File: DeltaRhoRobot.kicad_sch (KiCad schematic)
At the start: 44 parts, among them J11 Conn_01x02_Socket, J5 USB_C_Receptacle_USB2.0, J6 USB_C_Receptacle_USB2.0, SW1 CAS-120A1, U2 AMS1117-3.3, U7 TPS566242DRLR

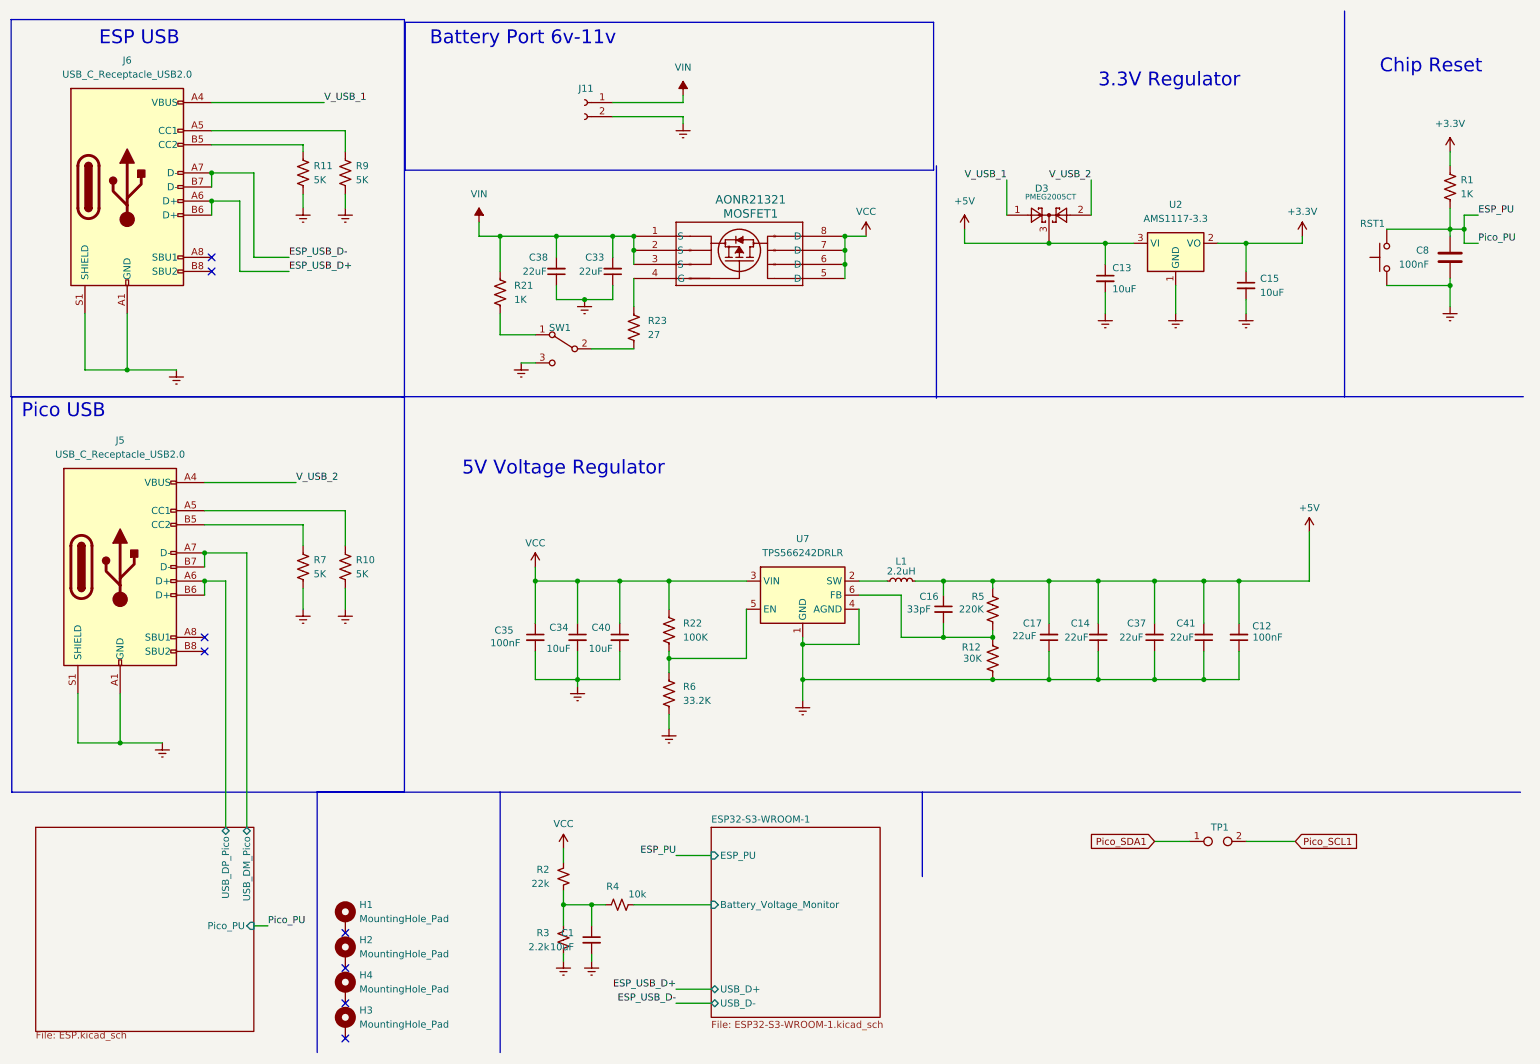
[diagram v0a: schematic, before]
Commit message: Fixed reference errors and bootstrap pin assignments
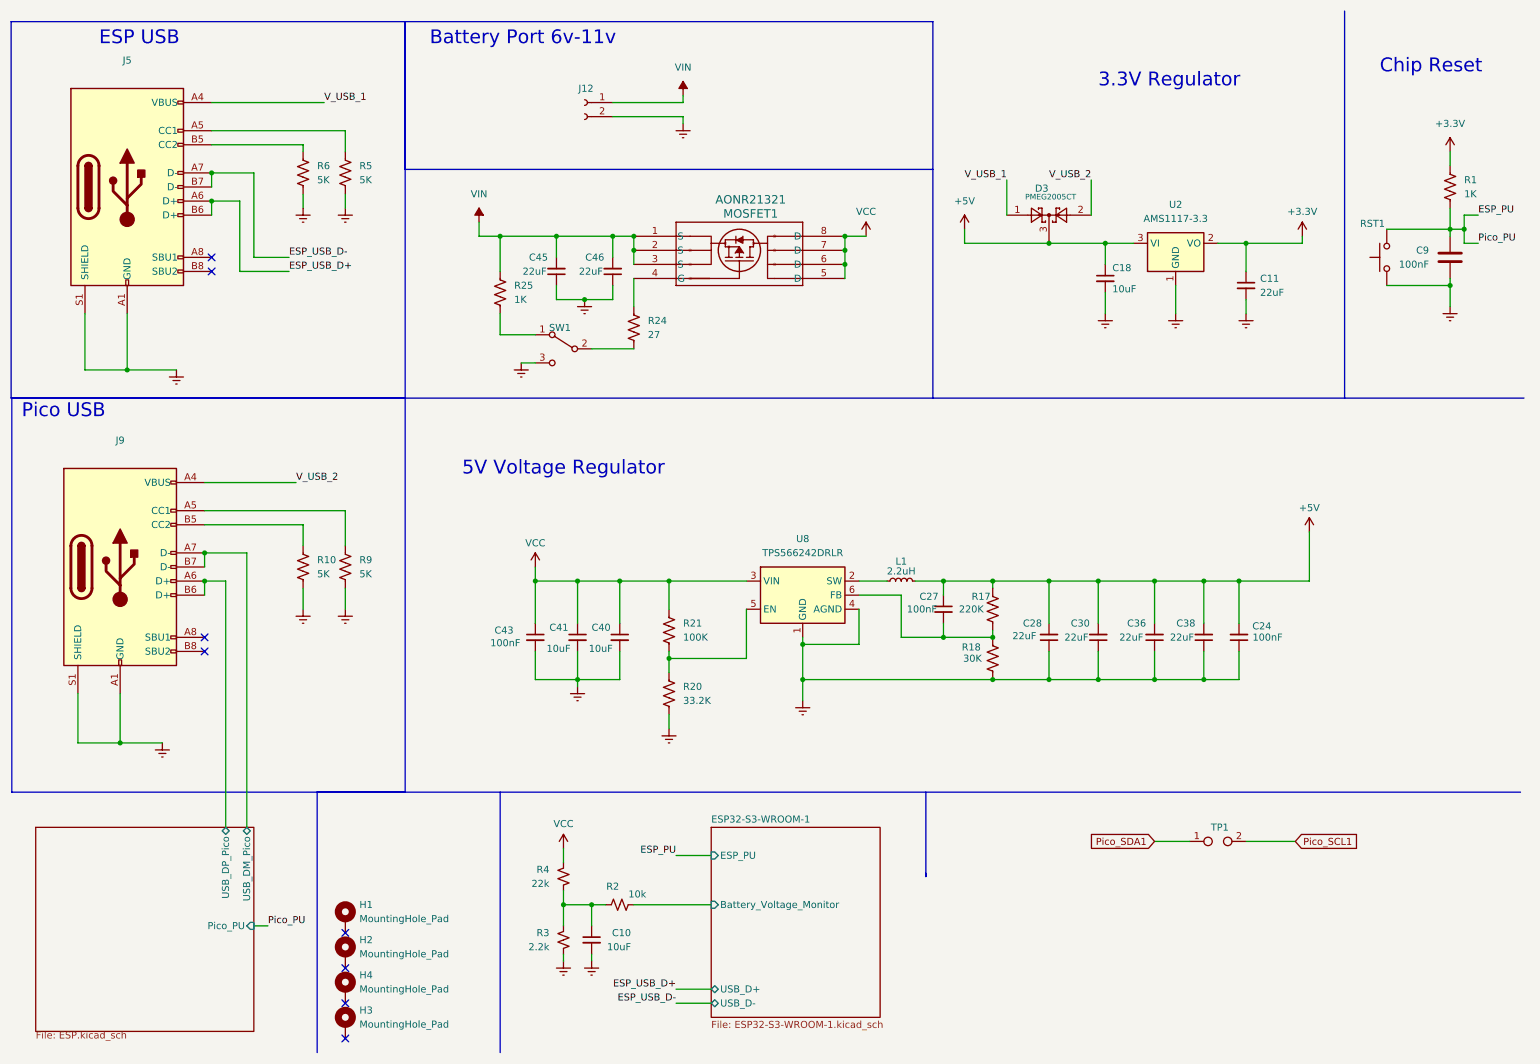
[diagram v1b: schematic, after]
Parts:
- C11: renamed from C15; value 10uF -> 22uF; footprint Capacitor_SMD:C_1206_3216Metric -> Capacitor_SMD:C_0805_2012Metric
- C27: renamed from C16; value 33pF -> 100nF; LCSC Part # C1562 -> C307331
- renumbered C1 to C10, C13 to C18, C12 to C24, C17 to C28, C14 to C30, C37 to C36, C41 to C38, C34 to C41, C35 to C43, C38 to C45, C33 to C46, C8 to C9, J11 to J12, J6 to J5, J5 to J9, R7 to R10, R5 to R17, R12 to R18, R4 to R2, R6 to R20, R22 to R21, R23 to R24, R21 to R25, R2 to R4, R9 to R5, R11 to R6, R10 to R9, U7 to U8

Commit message: Commit message
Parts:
- C11: LCSC Part # C13585 -> C45783
- C28: LCSC Part # C45783 -> C45783
- C40, C41: LCSC Part # C1525 -> C15525
- R17: LCSC Part # (none) -> C22961
